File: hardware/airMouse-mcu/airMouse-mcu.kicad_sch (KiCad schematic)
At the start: 57 parts, among them J1 MCU_PRG, J2 RADIO_PRG, J3 AT, Q1 IRLML6346, SW1 KEY, U1 LSM6DS3TR-C, U2 MCP1640CT-I/CHY, U3 STM32G071RBTx, U4 ESP32-C3-WROOM-02U

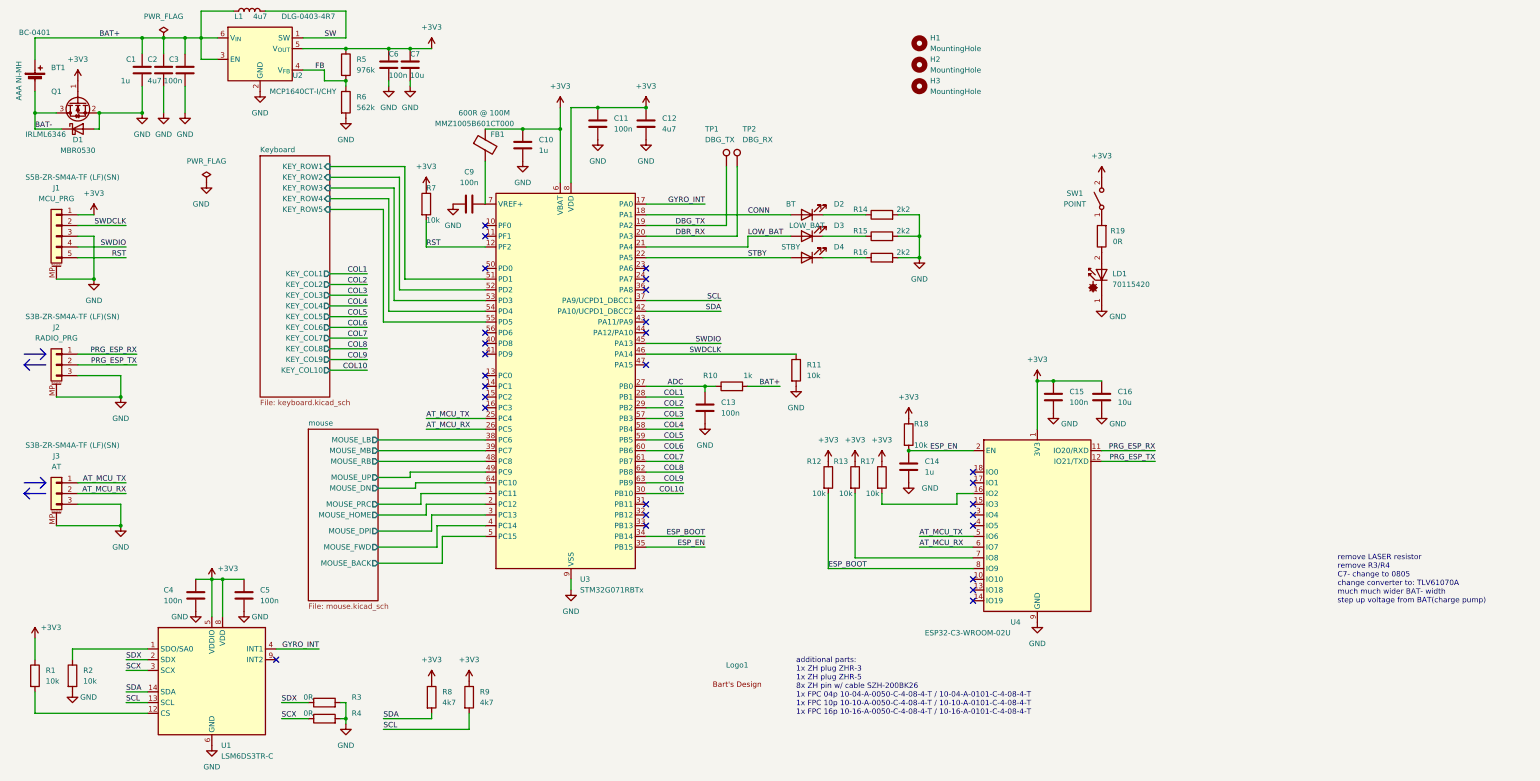
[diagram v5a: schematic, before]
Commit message: fixed receiving data- overrun turned off
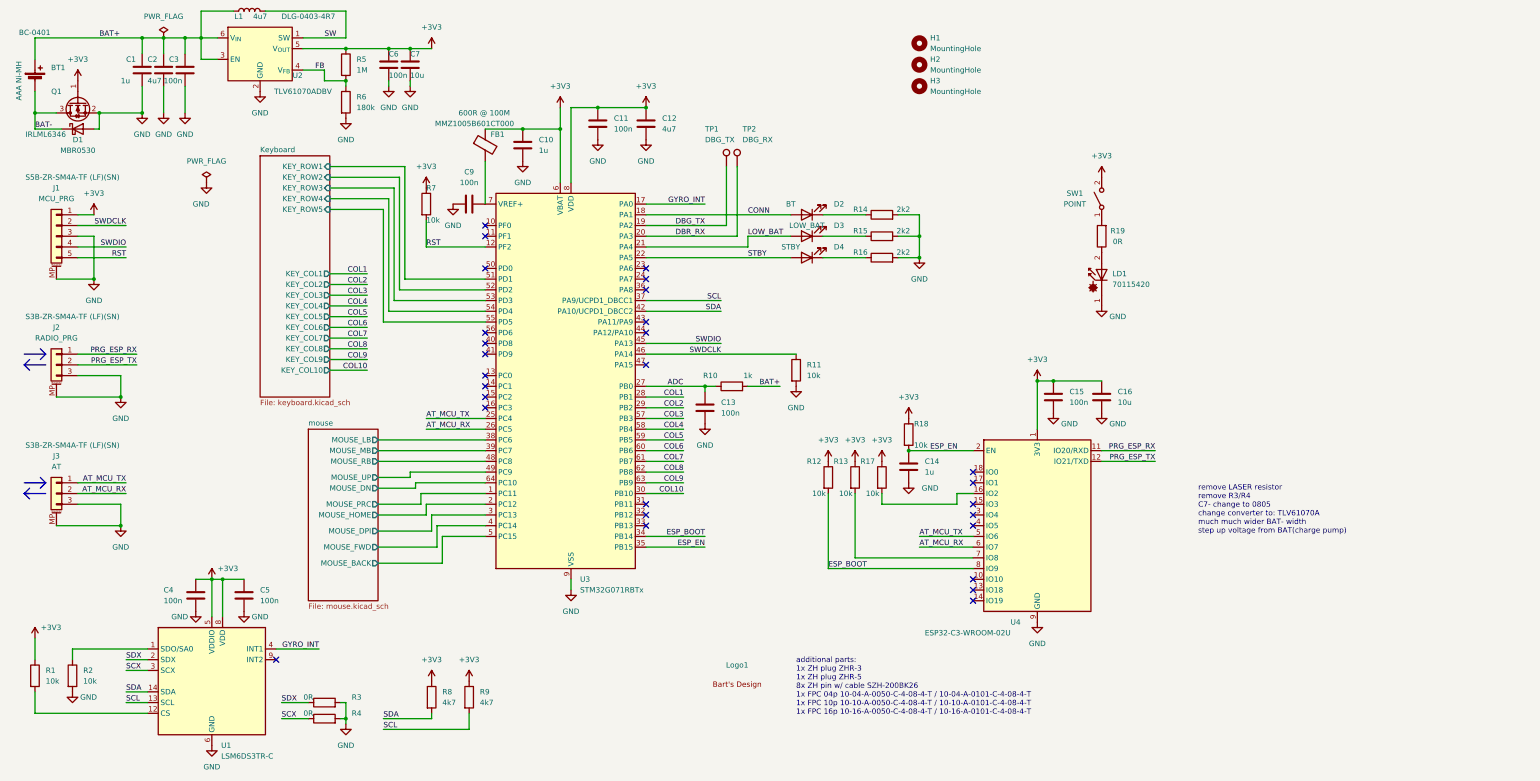
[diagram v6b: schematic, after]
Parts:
- R5: value 976k -> 1M
- R6: value 562k -> 180k
- U2: value MCP1640CT-I/CHY -> TLV61070ADBV; symbol Regulator_Switching:MCP1640Cx-xCHY -> Regulator_Switching:TLV61070ADBV
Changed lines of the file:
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@@
 	(text "remove LASER resistor\nremove R3/R4\nC7- change to 0805\nchange converter to: TLV61070A\nmuch much wider BAT- width\nstep up voltage from BAT(charge pump)"
 		(exclude_from_sim no)
-		(at 326.39 148.59 0)
+		(at 293.37 132.08 0)
 		(effects
 			(font
@@
 	)
 	(symbol
-		(lib_id "Regulator_Switching:MCP1640Cx-xCHY")
+		(lib_id "Regulator_Switching:TLV61070ADBV")
 		(at 71.12 25.4 0)
 		(unit 1)
@@
 			)
 		)
-		(property "Value" "MCP1640CT-I/CHY"
+		(property "Value" "TLV61070ADBV"
 			(at 81.28 33.02 0)
 			(effects
@@
 			)
 		)
-		(property "Datasheet" "http://ww1.microchip.com/downloads/en/DeviceDoc/20002234D.pdf"
-			(at 64.77 13.97 0)
+		(property "Datasheet" "https://www.ti.com/lit/ds/symlink/tlv61070a.pdf"
+			(at 71.12 12.7 0)
 			(effects
 				(font
@@
 			)
 		)
-		(property "Description" "Synchronous Boost Regulator, Adjustable Output 2.0V-5.5V, PWM/PFM Input to Output Bypass, SOT-23"
+		(property "Description" "Boost Converter, 2.5A switch current limit, 2.2-5.5V Output Voltage, 0.5-5.5V Input Voltage, SOT-23-6"
 			(at 71.12 25.4 0)
 			(effects
@@
 			)
 		)
-		(property "Value" "976k"
+		(property "Value" "1M"
 			(at 93.98 27.9399 0)
 			(effects
@@
 			)
 		)
-		(property "Value" "562k"
+		(property "Value" "180k"
 			(at 93.98 36.8299 0)
 			(effects

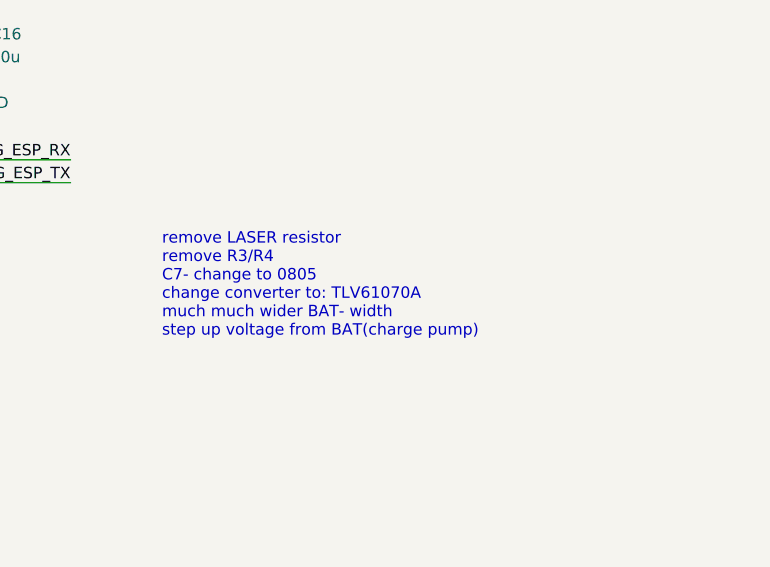
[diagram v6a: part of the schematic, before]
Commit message: improved keyboard library
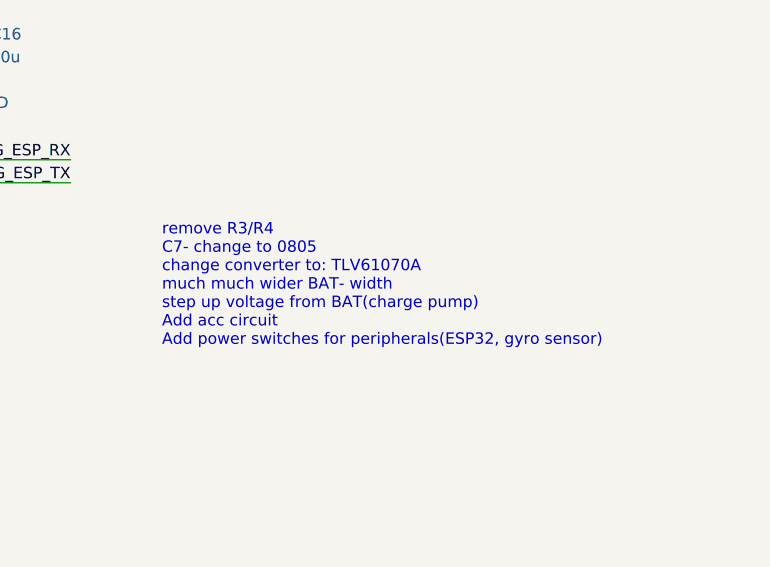
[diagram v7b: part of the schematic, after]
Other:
- note added: "remove R3/R4 C7- change to 0805 change converter to: TLV61070A much much wider BAT- width step up voltage from BAT(charge pump) Add acc circuit Add power switches for peripherals(ESP32, gyro sensor)"
- note removed: "remove LASER resistor remove R3/R4 C7- change to 0805 change converter to: TLV61070A much much wider BAT- width step up voltage from BAT(charge pump)"
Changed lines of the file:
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@@
 		)
 	)
-	(text "remove LASER resistor\nremove R3/R4\nC7- change to 0805\nchange converter to: TLV61070A\nmuch much wider BAT- width\nstep up voltage from BAT(charge pump)"
+	(text "remove R3/R4\nC7- change to 0805\nchange converter to: TLV61070A\nmuch much wider BAT- width\nstep up voltage from BAT(charge pump)\nAdd acc circuit\nAdd power switches for peripherals(ESP32, gyro sensor)"
 		(exclude_from_sim no)
 		(at 293.37 132.08 0)

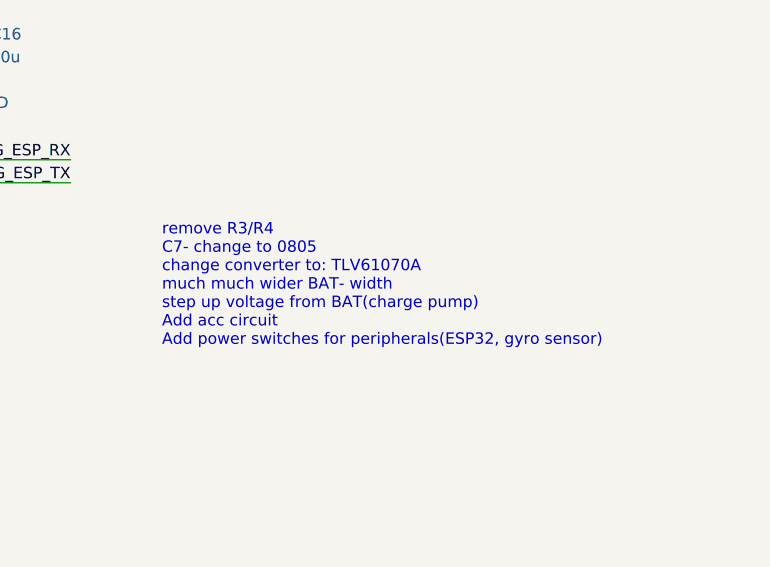
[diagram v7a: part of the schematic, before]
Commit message: included esp-at firmware sources, and binaries fixed polling rate on linux
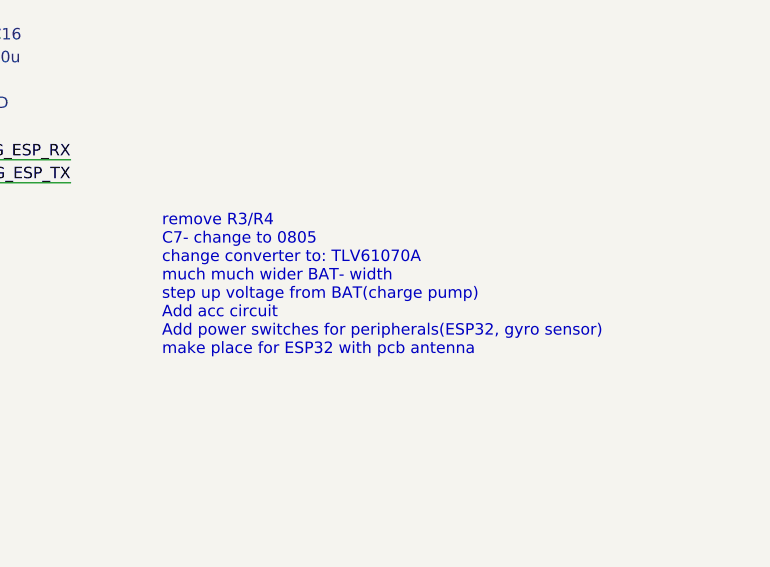
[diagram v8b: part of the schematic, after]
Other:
- note added: "remove R3/R4 C7- change to 0805 change converter to: TLV61070A much much wider BAT- width step up voltage from BAT(charge pump) Add acc circuit Add power switches for peripherals(ESP32, gyro sensor) make place for ESP32 with pcb antenna"
- note removed: "remove R3/R4 C7- change to 0805 change converter to: TLV61070A much much wider BAT- width step up voltage from BAT(charge pump) Add acc circuit Add power switches for peripherals(ESP32, gyro sensor)"
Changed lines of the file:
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@@
 		)
 	)
-	(text "remove R3/R4\nC7- change to 0805\nchange converter to: TLV61070A\nmuch much wider BAT- width\nstep up voltage from BAT(charge pump)\nAdd acc circuit\nAdd power switches for peripherals(ESP32, gyro sensor)"
+	(text "remove R3/R4\nC7- change to 0805\nchange converter to: TLV61070A\nmuch much wider BAT- width\nstep up voltage from BAT(charge pump)\nAdd acc circuit\nAdd power switches for peripherals(ESP32, gyro sensor)\nmake place for ESP32 with pcb antenna"
 		(exclude_from_sim no)
 		(at 293.37 132.08 0)
